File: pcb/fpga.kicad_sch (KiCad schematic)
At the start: 0 parts

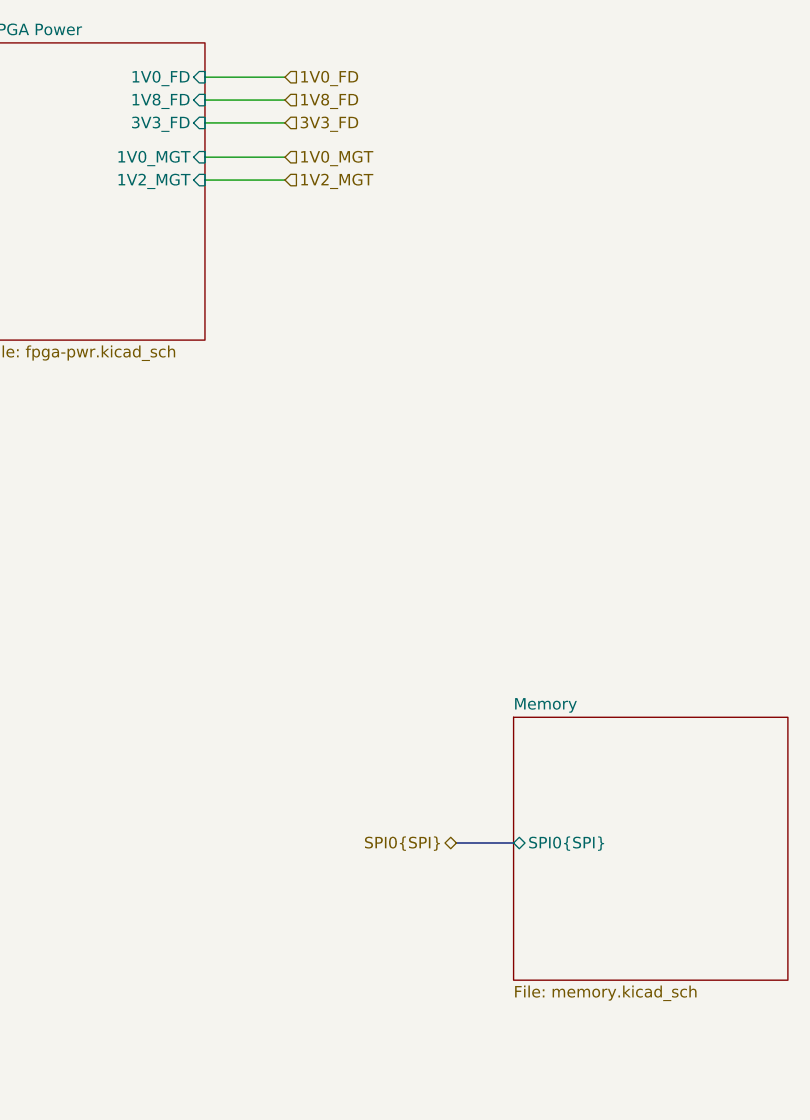
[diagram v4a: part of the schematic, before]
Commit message: current sense hierarchy definition
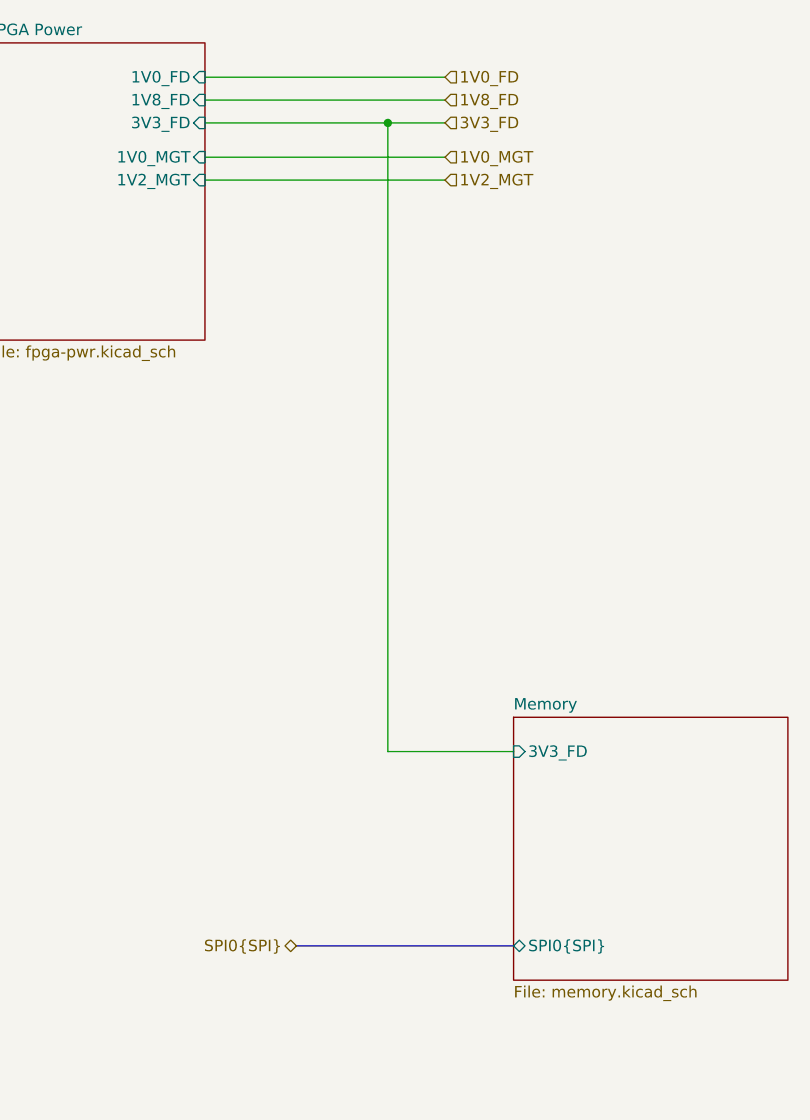
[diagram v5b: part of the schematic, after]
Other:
- sheet Memory ports: added 3V3_FD; removed none
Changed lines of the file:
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@@
 		(company "Andre S Winkel")
 	)
+	(junction
+		(at 63.5 27.94)
+		(diameter 0)
+		(color 0 0 0 0)
+	)
 	(bus_entry
 		(at 175.26 116.84)
@@
 	(wire
 		(pts
-			(xy 52.07 27.94) (xy 43.18 27.94)
-		)
-		(stroke
-			(width 0)
-			(type default)
-		)
-	)
-	(wire
-		(pts
-			(xy 52.07 22.86) (xy 43.18 22.86)
+			(xy 69.85 22.86) (xy 43.18 22.86)
 		)
 		(stroke
@@
 	(wire
 		(pts
-			(xy 52.07 31.75) (xy 43.18 31.75)
+			(xy 63.5 27.94) (xy 69.85 27.94)
+		)
+		(stroke
+			(width 0)
+			(type default)
+		)
+	)
+	(wire
+		(pts
+			(xy 69.85 31.75) (xy 43.18 31.75)
 		)
 		(stroke
@@
 	(wire
 		(pts
-			(xy 52.07 25.4) (xy 43.18 25.4)
+			(xy 69.85 25.4) (xy 43.18 25.4)
 		)
 		(stroke
@@
 		)
 	)
+	(wire
+		(pts
+			(xy 63.5 27.94) (xy 63.5 97.79)
+		)
+		(stroke
+			(width 0)
+			(type default)
+		)
+	)
+	(wire
+		(pts
+			(xy 43.18 27.94) (xy 63.5 27.94)
+		)
+		(stroke
+			(width 0)
+			(type default)
+		)
+	)
+	(wire
+		(pts
+			(xy 63.5 97.79) (xy 77.47 97.79)
+		)
+		(stroke
+			(width 0)
+			(type default)
+		)
+	)
 	(bus
 		(pts
@@
 	(bus
 		(pts
-			(xy 71.12 107.95) (xy 77.47 107.95)
-		)
-		(stroke
-			(width 0)
-			(type default)
-		)
-	)
-	(wire
-		(pts
-			(xy 52.07 34.29) (xy 43.18 34.29)
+			(xy 53.34 119.38) (xy 77.47 119.38)
+		)
+		(stroke
+			(width 0)
+			(type default)
+		)
+	)
+	(wire
+		(pts
+			(xy 69.85 34.29) (xy 43.18 34.29)
 		)
 		(stroke
@@
 	(hierarchical_label "1V0_MGT"
 		(shape input)
-		(at 52.07 31.75 0)
+		(at 69.85 31.75 0)
 		(effects
 			(font
@@
 	(hierarchical_label "1V2_MGT"
 		(shape input)
-		(at 52.07 34.29 0)
+		(at 69.85 34.29 0)
 		(effects
 			(font
@@
 	(hierarchical_label "1V0_FD"
 		(shape input)
-		(at 52.07 22.86 0)
+		(at 69.85 22.86 0)
 		(effects
 			(font
@@
 	(hierarchical_label "1V8_FD"
 		(shape input)
-		(at 52.07 25.4 0)
+		(at 69.85 25.4 0)
 		(effects
 			(font
@@
 	(hierarchical_label "SPI0{SPI}"
 		(shape bidirectional)
-		(at 71.12 107.95 180)
+		(at 53.34 119.38 180)
 		(effects
 			(font
@@
 	(hierarchical_label "3V3_FD"
 		(shape input)
-		(at 52.07 27.94 0)
+		(at 69.85 27.94 0)
 		(effects
 			(font
@@
 		)
 		(pin "SPI0{SPI}" bidirectional
-			(at 77.47 107.95 180)
-			(effects
-				(font
+			(at 77.47 119.38 180)
+			(effects
+				(font
+					(size 1.27 1.27)
+				)
+				(justify left)
+			)
+		)
+		(pin "3V3_FD" input
+			(at 77.47 97.79 180)
+			(effects
+				(font

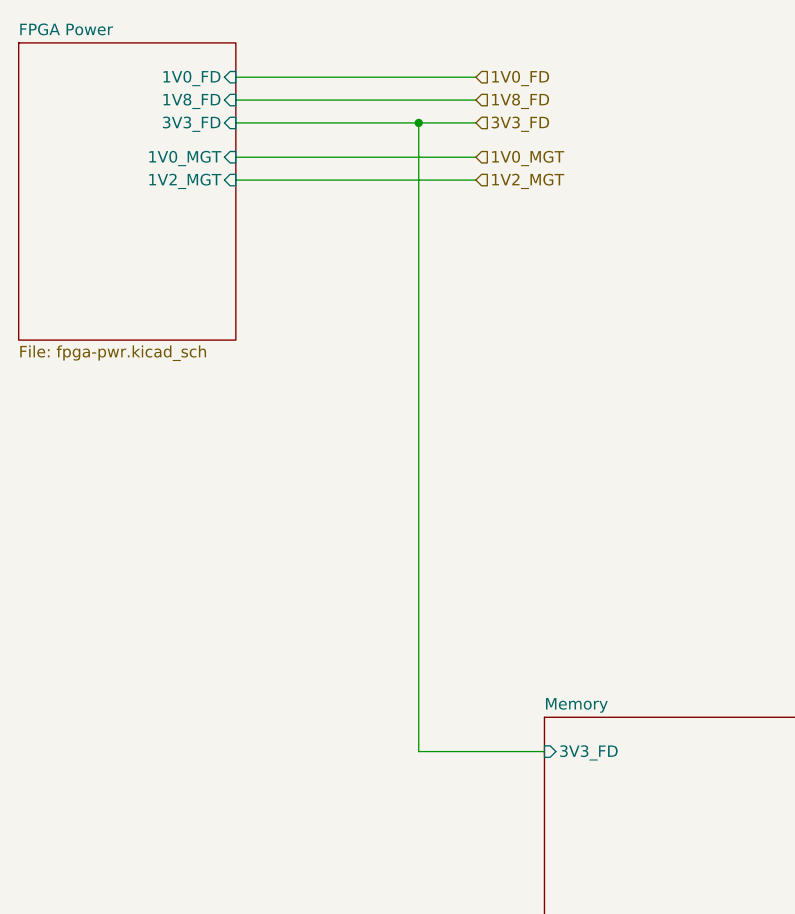
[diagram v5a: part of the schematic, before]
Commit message: power flags
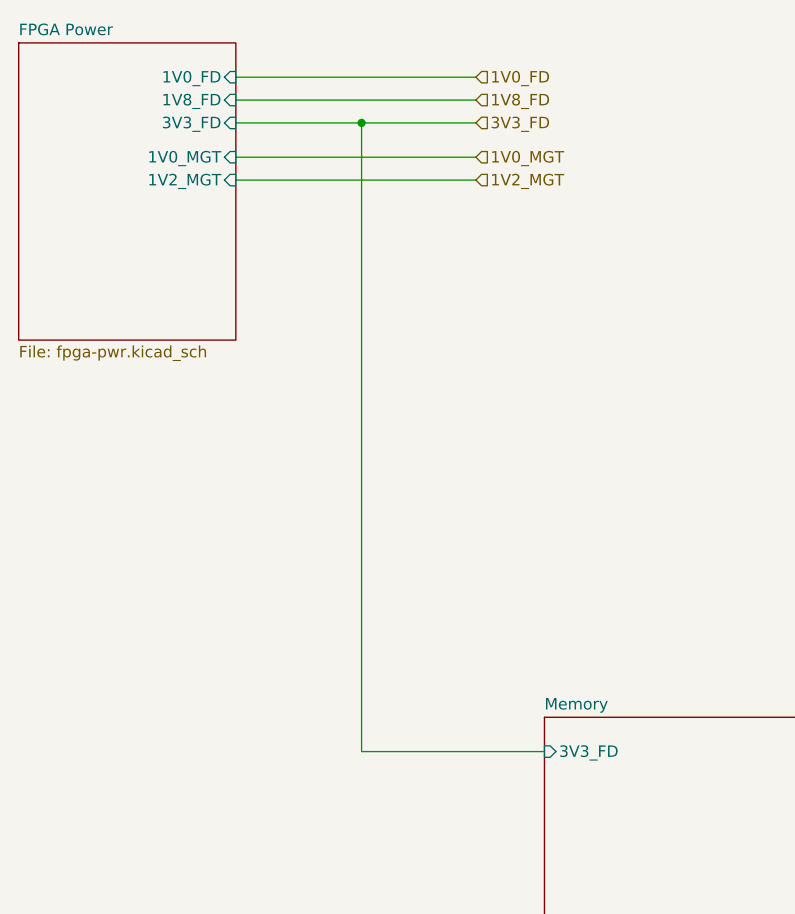
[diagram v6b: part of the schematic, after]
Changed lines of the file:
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@@
 	)
 	(junction
-		(at 63.5 27.94)
+		(at 57.15 27.94)
 		(diameter 0)
 		(color 0 0 0 0)
@@
 	(wire
 		(pts
-			(xy 63.5 27.94) (xy 69.85 27.94)
+			(xy 57.15 27.94) (xy 69.85 27.94)
 		)
 		(stroke
@@
 	(wire
 		(pts
-			(xy 63.5 27.94) (xy 63.5 97.79)
-		)
-		(stroke
-			(width 0)
-			(type default)
-		)
-	)
-	(wire
-		(pts
-			(xy 43.18 27.94) (xy 63.5 27.94)
-		)
-		(stroke
-			(width 0)
-			(type default)
-		)
-	)
-	(wire
-		(pts
-			(xy 63.5 97.79) (xy 77.47 97.79)
-		)
-		(stroke
+			(xy 57.15 27.94) (xy 57.15 97.79)
+		)
+		(stroke
+			(width 0)
+			(type default)
+		)
+	)
+	(wire
+		(pts
+			(xy 43.18 27.94) (xy 57.15 27.94)
+		)
+		(stroke
+			(width 0)
+			(type default)
+		)
+	)
+	(wire
+		(pts
+			(xy 57.15 97.79) (xy 77.47 97.79)
+		)
+		(stroke

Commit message: pcie definitions
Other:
- sheet FPGA 3 ports: added PCIE.F2P_N, PCIE.F2P_P, PCIE.P2F_N, PCIE.P2F_P; removed PCIE.RX_N, PCIE.RX_P, PCIE.TX_N, PCIE.TX_P

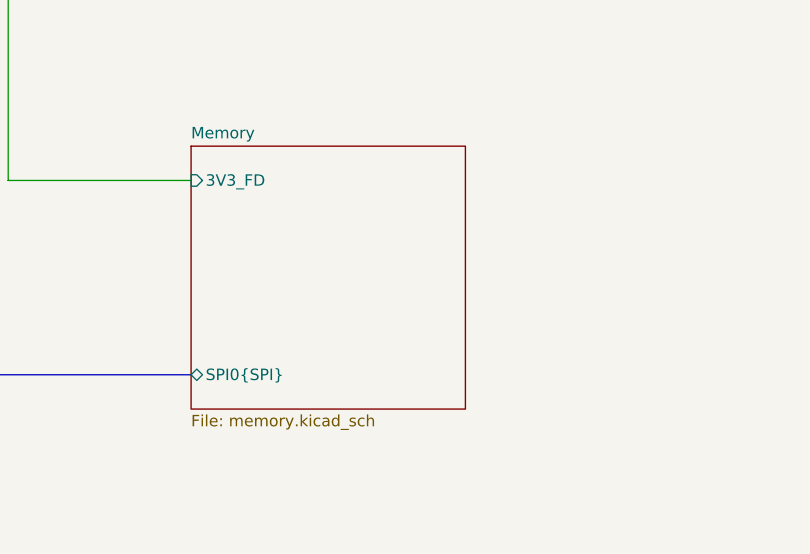
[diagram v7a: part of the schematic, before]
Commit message: added dram, defined pcie sideband sigs.
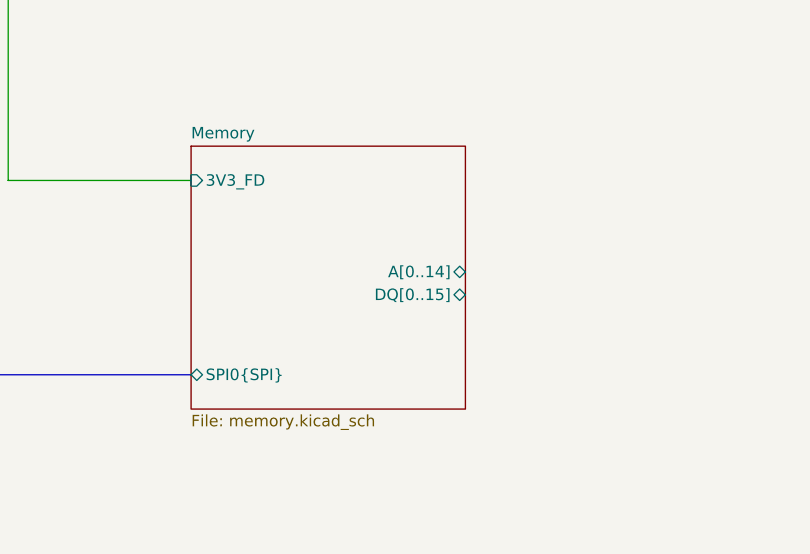
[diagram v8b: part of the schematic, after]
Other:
- sheet Memory ports: added A[0..14], DQ[0..15]; removed none
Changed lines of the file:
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@@
+			)
+		)
+		(pin "A[0..14]" bidirectional
+			(at 107.95 107.95 0)
+			(effects
+				(font
+					(size 1.27 1.27)
+				)
+				(justify right)
+			)
+		)
+		(pin "DQ[0..15]" bidirectional
+			(at 107.95 110.49 0)
+			(effects
+				(font
+					(size 1.27 1.27)
+				)
+				(justify right)
 			)
 		)
